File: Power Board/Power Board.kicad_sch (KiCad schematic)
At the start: 149 parts, among them IC1 LTC4151IMS#PBF, J1 Conn_01x02, J10 Conn_01x02, J11 Conn_01x02, J12 Conn_01x02, J13 Conn_01x02, J14 Conn_01x02, J15 Conn_01x02, J16 Conn_01x02, J17 Conn_01x02, J19 Conn_01x04, J2 Conn_01x02, J20 Conn_01x04, J3 Conn_01x02, J4 Conn_01x02, J5 Conn_01x02, J6 Conn_01x02, J7 Conn_01x02, J8 Conn_01x02, Q1 Q_PMOS_GDS, Q10 Q_NMOS_GDS, Q11 Q_NMOS_GDS, Q12 Q_NMOS_GDS, Q13 Q_NMOS_GDS, Q14 Q_NMOS_GDS, Q15 Q_NMOS_GDS, Q16 Q_NMOS_GDS, Q17 Q_NMOS_GDS, Q18 Q_NMOS_GDS, Q19 Q_NMOS_GDS, Q2 Q_PMOS_GDS, Q20 Q_NMOS_GDS, Q21 Q_NMOS_GDS, Q22 Q_NMOS_GDS, Q3 Q_PMOS_GDS, Q4 Q_PMOS_GDS, Q5 Q_PMOS_GDS, Q6 Q_PMOS_GDS, Q7 Q_PMOS_GDS, Q8 Q_PMOS_GDS, Q9 Q_NMOS_GDS, SW1 SW_Push_DPDT, U1 TLV70033_SOT23-5, U11 ACS770xCB-200U-PFF, U12 ADC128S052CIMT, U2 LTC4372CDD-PBF, U3 LTC4372CDD-PBF, U4 LTC4372CDD-PBF, U5 LTC4372CDD-PBF, U6 LTC4372CDD-PBF, U7 LTC4372CDD-PBF, U8 ADC128S052CIMT, U9 LTC4372CDD-PBF

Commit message: separated current sensors and updated ADCs, component numbering
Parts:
- removed C10: 10 uF, Capacitor_SMD:C_0201_0603Metric_Pad0.64x0.40mm_HandSolder, symbol Device:C
- removed J_Motor1, J_Motor2: Conn_01x02, Connector_AMASS:AMASS_XT60PW-F_1x02_P7.20mm_Horizontal, symbol Connector_Generic:Conn_01x02
- removed U11: ACS770xCB-200U-PFF, Sensor_Current:Allegro_CB_PFF, symbol Sensor_Current:ACS770xCB-200U-PFF
- added C30, C32, C34, C36, C38, C40: 0.1 uF, Capacitor_SMD:C_0201_0603Metric_Pad0.64x0.40mm_HandSolder, symbol Device:C
- added C31, C33, C35, C37, C39, C41: 1 uF, Capacitor_SMD:C_0201_0603Metric_Pad0.64x0.40mm_HandSolder, symbol Device:C
- added C42, C43, C44, C45, C46, C47, C48, C49, C50, C51, C52, C56: 22 nF, Capacitor_SMD:C_0201_0603Metric_Pad0.64x0.40mm_HandSolder, symbol Device:C
- added J_24_MONITOR1: Conn_01x02, symbol Connector_Generic:Conn_01x02
- added R43, R44, R45, R46, R47, R48, R49, R50, R51, R52: 100, Resistor_SMD:R_0805_2012Metric_Pad1.20x1.40mm_HandSolder, symbol Device:R
- added U10, U11, U12, U13, U14, U8, U9: ACS770xCB-050U-PFF, Sensor_Current:Allegro_CB_PFF, symbol Sensor_Current:ACS770xCB-050U-PFF
- R34: value 20k -> 100
- R35: value 10k -> 100
- renumbered J_PDB1 to J_BUS1, Q17 to Q10, Q13 to Q11, Q14 to Q12, Q9 to Q13, Q10 to Q14, Q11 to Q15, Q12 to Q16, Q21 to Q17, Q22 to Q18, Q15 to Q19, Q16 to Q20, Q19 to Q21, Q20 to Q22, Q18 to Q9, U9 to U1, U8 to U15, U12 to U16, U1 to U17, U4 to U2, U2 to U3, U3 to U4, U7 to U5, U5 to U6, U6 to U7
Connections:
- net +5V is gone; now on net 5V_REGULATED: C22.1, C23.1
- net 24V_MONITOR_SCL: now also J_24_MONITOR1.1 (Pin_1)
- net 24V_MONITOR_SDA: now also J_24_MONITOR1.2 (Pin_2)
- net 5V_REGULATED: now also C30.1, C31.1, C32.1, C33.1, C34.1, C35.1, C36.1, C37.1, C38.1, C39.1, C40.1, C41.1, U10.1 (VCC), U11.1 (VCC), U12.1 (VCC), U13.1 (VCC), U14.1 (VCC), U8.1 (VCC), U9.1 (VCC)
- net GND: now also C30.2, C31.2, C32.2, C33.2, C34.2, C35.2, C36.2, C37.2, C38.2, C39.2, C40.2, C41.2, C42.2, C43.2, C44.2, C45.2, C46.2, C47.2, C48.2, C49.2, C50.2, C51.2, C52.2, C56.2, U10.2 (GND), U11.2 (GND), U12.2 (GND), U13.2 (GND), U14.2 (GND), U8.2 (GND), U9.2 (GND); no longer R35.2
- net THERM_1: now also R49.1; no longer U16.4 (IN0)
- net THERM_2: now also R46.1; no longer U16.5 (IN1)
- net THERM_3: now also R47.1; no longer U16.6 (IN2)
- net THERM_4: now also R48.1; no longer U16.7 (IN3)
- net THERM_5: now also R50.1; no longer U16.8 (IN4)
- net THERM_6: now also R51.1; no longer U16.9 (IN5)
- net THERM_7: now also R52.1; no longer U16.10 (IN6)
- net THERM_8: no longer U16.11 (IN7)
- net at U15.10 (IN6): now also C46.1, R45.2
- net at U15.6 (IN2): now also R34.2, C42.1
- net at U15.7 (IN3): now also R35.2, C43.1
- net at U15.8 (IN4): now also C44.1, R43.2
- net at U15.9 (IN5): now also C45.1, R44.2
- net 12V_AMP_SENSE renamed BATT_1_SENSE
- net BATT_1_SENSE: now also U8.3 (VIOUT)
- removed net 12V_PRESENSE: Q11.2 (D), Q13.2 (D), Q15.2 (D), Q17.2 (D), Q19.2 (D), Q21.2 (D), Q9.2 (D), R34.1, U1.1 (OUT), U2.1 (OUT), U3.1 (OUT), U4.1 (OUT), U5.1 (OUT), U7.1 (OUT)
- net 12V_UNREGULATED: no longer names the net of J_BUS1.2 (Pin_2)
- new net: C47.1, R46.2, U16.5 (IN1)
- new net: C52.1, R51.2, U16.9 (IN5)
- new net: C51.1, R50.2, U16.8 (IN4)
- new net: C56.1, R52.2, U16.10 (IN6)
- new net: C50.1, R49.2, U16.4 (IN0)
- new net: C48.1, R47.2, U16.6 (IN2)
- new net: C49.1, R48.2, U16.7 (IN3)
- new net BATT_1: U8.5 (IP-)
- new net BATT_1_PRESENSE: Q9.2 (D), U1.1 (OUT), U8.4 (IP+)
- new net BATT_2: U9.5 (IP-)
- new net BATT_2_PRESENSE: Q11.2 (D), U2.1 (OUT), U9.4 (IP+)
- new net BATT_2_SENSE: R2.1, U9.3 (VIOUT)
- new net BATT_3: U10.5 (IP-)
- new net BATT_3_PRESENSE: Q13.2 (D), U10.4 (IP+), U3.1 (OUT)
- new net BATT_3_SENSE: R34.1, U10.3 (VIOUT)
- new net BATT_4: U11.5 (IP-)
- new net BATT_4_PRESENSE: Q15.2 (D), U11.4 (IP+), U4.1 (OUT)
- new net BATT_4_SENSE: R35.1, U11.3 (VIOUT)
- new net BATT_5: U12.5 (IP-)
- new net BATT_5_PRESENSE: Q17.2 (D), U12.4 (IP+), U5.1 (OUT)
- new net BATT_5_SENSE: R43.1, U12.3 (VIOUT)
- new net BATT_6: U13.5 (IP-)
- new net BATT_6_PRESENSE: Q19.2 (D), U13.4 (IP+)
- new net BATT_6_SENSE: R44.1, U13.3 (VIOUT)
- new net BATT_7: U14.5 (IP-)
- new net BATT_7_PRESENSE: Q21.2 (D), U14.4 (IP+), U7.1 (OUT)
- new net BATT_7_SENSE: R45.1, U14.3 (VIOUT)
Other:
- note added: "Current Monitors"
- moved on the sheet: C2, C21, C22, C23, C26, C27, IC1, J10, J11, J12, J13, J14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

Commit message: updated schematic numbering, made rough PCB design for battery 1
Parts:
- renumbered C11 to C1, C17 to C10, C8 to C11, C14 to C12, C9 to C13, C15 to C14, C2 to C15, C1 to C16, C42 to C17, C43 to C18, C44 to C19, C12 to C2, C45 to C20, C46 to C21, C20 to C22, C18 to C23, C19 to C24, C50 to C25, C47 to C26, C48 to C27, C49 to C28, C51 to C29, C7 to C3, C52 to C30, C56 to C31, C21 to C32, C26 to C33, C27 to C34, C22 to C35, C23 to C36, C30 to C37, C31 to C38, C40 to C39, C13 to C4, C41 to C40, C32 to C41, C33 to C42, C34 to C43, C35 to C44, C36 to C45, C37 to C46, C38 to C47, C39 to C48, C28 to C49, C3 to C5, C29 to C50, C25 to C51, C24 to C52, C4 to C6, C5 to C7, C6 to C8, C16 to C9, R5 to R1, R21 to R10, R22 to R11, R19 to R12, R25 to R13, R28 to R14, R13 to R15, R14 to R16, R15 to R17, R16 to R18, R17 to R19, R6 to R2, R18 to R20, R31 to R21, R32 to R22, R33 to R23, R23 to R24, R26 to R25, R29 to R26, R24 to R27, R27 to R28, R30 to R29, R7 to R3, R8 to R4, R9 to R5, R10 to R6, R11 to R7, R12 to R8, R20 to R9, R3 to RA1, R47 to RA10, R48 to RA11, R50 to RA12, R51 to RA13, R52 to RA14, R2 to RA2, R34 to RA3, R35 to RA4, R43 to RA5, R44 to RA6, R45 to RA7, R49 to RA8, R46 to RA9, R1 to RI1, R4 to RT1, R36 to RT2, R37 to RT3, R38 to RT4, R39 to RT5, R40 to RT6, R41 to RT7, R42 to RT8

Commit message: adc design on power board
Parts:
- removed C51, C52: UVZ2A331MHD1TO, UVZ2A331MHD:CAP_UEP_12P5X25_NCH, symbol 2025-11-07_01-42-20:UVZ2A331MHD1TO
- added C51, C52: EEV-TG2A331M, EEV_TG2A331M:CAP_SMD_19X19_PAN, symbol EEV_TG2A331M:EEV-TG2A331M
- added NT1: NetTie_2, symbol Device:NetTie_2
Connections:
- net 24V_PRESENSE is gone; now on net 24V_PSO: IC1.1 (SENSE+), IC1.2 (VIN), IC1.3 (ADR1), RI1.1
- net 24_REGULATED is gone; now on net 24V_REGULATED: PS1.4 (+VOUT)
- net 24V_UNREGULATED: now also C51.2, C52.1
- net GND: now also C23.2, C24.2, C33.2, C34.2, C51.1, C52.2, NT1.1
- net GNDD: now also NT1.2

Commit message: laid out most components, reworked battery 1 pours, made connections for ADCs; buck converter layout and routing in progress
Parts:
- removed Q1, Q2, Q3, Q4, Q5, Q6, Q7, Q8: Q_PMOS_GDS, Package_SO:PowerPAK_SO-8_Single, symbol Device:Q_PMOS_GDS
- added Q1, Q2, Q3, Q4, Q5, Q6, Q7, Q8: Q_PMOS_GDS, Package_SO:PowerPAK_SO-8_Single, symbol Transistor_FET:Q_PMOS_GDS
- Q10, Q11, Q12, Q13, Q14, Q15, Q16, Q17, Q18, Q19, Q20, Q21, Q22, Q9: footprint Package_TO_SOT_SMD:TDSON-8-1 -> Package_SO:PowerPAK_SO-8_Single
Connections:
- net 24V_PSO: now also Q8.3 (S)
- net ADC_1_DIN: now also J20.4 (Pin_4); no longer J20.3 (Pin_3)
- net ADC_1_DOUT: now also J20.2 (Pin_2); no longer J20.4 (Pin_4)
- net ADC_1_SCLK: now also J20.3 (Pin_3); no longer J20.2 (Pin_2)
- net ADC_2_DIN: now also J19.4 (Pin_4); no longer J19.3 (Pin_3)
- net ADC_2_DOUT: now also J19.2 (Pin_2); no longer J19.4 (Pin_4)
- net ADC_2_SCLK: now also J19.3 (Pin_3); no longer J19.2 (Pin_2)
- net BATT_IN_12_1: now also Q1.3 (S)
- net BATT_IN_12_2: now also Q2.3 (S)
- net BATT_IN_12_3: now also Q3.3 (S)
- net BATT_IN_12_4: now also Q4.3 (S)
- net BATT_IN_12_5: now also Q5.3 (S)
- net BATT_IN_12_6: now also Q6.3 (S)
- net BATT_IN_12_7: now also Q7.3 (S)
- net GND: now also U1.9 (GND), U2.9 (GND), U3.9 (GND), U4.9 (GND), U5.9 (GND), U6.9 (GND), U7.9 (GND); no longer C22.2, C32.2
- net GNDD: now also C22.2, C32.2
- net at D5.2 (A), R5.1: now also Q5.1 (G)
- net at F5.2: now also Q5.2 (D)
- net at D4.2 (A), R4.1: now also Q4.1 (G)
- net at F8.2: now also Q8.2 (D)
- net at F7.2: now also Q7.2 (D)
- net at D7.2 (A), R7.1: now also Q7.1 (G)
- net at D3.2 (A), R3.1: now also Q3.1 (G)
- net at D6.2 (A), R6.1: now also Q6.1 (G)
- net at D8.2 (A), R8.1: now also Q8.1 (G)
- net at D1.2 (A), R1.1: now also Q1.1 (G)
- net at F1.2: now also Q1.2 (D)
- net at F4.2: now also Q4.2 (D)
- net at D2.2 (A), R2.1: now also Q2.1 (G)
- net at F2.2: now also Q2.2 (D)
- net at F3.2: now also Q3.2 (D)
- net at F6.2: now also Q6.2 (D)
- no-connect marks 0 -> 9
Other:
- moved on the sheet: C49, C50, U17

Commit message: changed ADC connectors, added series resistors
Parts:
- removed J19, J20: Conn_01x04, Connector_Molex:Molex_Micro-Fit_3.0_43045-0400_2x02_P3.00mm_Horizontal, symbol Connector_Generic:Conn_01x04
- added J18: Conn_02x03_Top_Bottom, Connector_Molex:Molex_Nano-Fit_105310-xx06_2x03_P2.50mm_Vertical, symbol Connector_Generic:Conn_02x03_Top_Bottom
- added J20, J9: Conn_02x03_Top_Bottom, Connector_Molex:Molex_Nano-Fit_105314-xx06_2x03_P2.50mm_Horizontal, symbol Connector_Generic:Conn_02x03_Top_Bottom
- added R30, R31, R32, R33, R34, R35, R36, R37: 33, Resistor_SMD:R_0805_2012Metric_Pad1.20x1.40mm_HandSolder, symbol Device:R
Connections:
- net 24V_PSO: now also C52.1, D9.1 (K), PS2.1 (+VIN), J18.1 (Pin_1)
- net 24V_UNREGULATED: now also J18.2 (Pin_2); no longer C52.1, D9.1 (K), PS2.1 (+VIN)
- net 5V_REG_SD: now also J18.6 (Pin_6)
- net ADC_1_CS: now also R30.2
- net ADC_1_DIN: now also R32.2
- net ADC_1_DOUT: now also R31.2
- net ADC_1_SCLK: now also R33.1
- net ADC_2_CS: now also R37.2
- net ADC_2_DIN: now also R35.2
- net ADC_2_DOUT: now also R36.2
- net ADC_2_SCLK: now also R34.1
- net GND: now also J18.4 (Pin_4)
- net GNDD: now also J20.2 (Pin_2), J20.5 (Pin_5), J9.2 (Pin_2), J9.5 (Pin_5)
- net SHDN: now also J18.5 (Pin_5)
- new net: J9.4 (Pin_4), R30.1
- new net: J9.1 (Pin_1), R33.2
- new net: J9.3 (Pin_3), R32.1
- new net: J20.3 (Pin_3), R35.1
- new net: J9.6 (Pin_6), R31.1
- new net: J20.1 (Pin_1), R34.2
- new net: J20.4 (Pin_4), R37.1
- new net: J20.6 (Pin_6), R36.1
- no-connect marks 9 -> 10
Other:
- moved on the sheet: SW1

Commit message: updated LTC4372s, switch connector, ADC; added some power planes for other batteries
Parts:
- removed SW1: SW_Push_DPDT, symbol Switch:SW_Push_DPDT
- added C53: 22 nF, Capacitor_SMD:C_0201_0603Metric_Pad0.64x0.40mm_HandSolder, symbol Device:C
- added RA15: 100, Resistor_SMD:R_0805_2012Metric_Pad1.20x1.40mm_HandSolder, symbol Device:R
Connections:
- net 24V_PSO: no longer C52.1, D9.1 (K), PS2.1 (+VIN)
- net 24V_UNREGULATED: now also C52.1, D9.1 (K), PS2.1 (+VIN)
- net BATT_IN_12_2: now also Q12.2 (D), U2.4 (IN); no longer Q14.2 (D), U3.4 (IN)
- net BATT_IN_12_3: now also Q14.2 (D), U3.4 (IN); no longer Q16.2 (D), U4.4 (IN)
- net BATT_IN_12_4: now also Q16.2 (D), U4.4 (IN); no longer Q12.2 (D), U2.4 (IN)
- net BATT_IN_12_5: now also Q18.2 (D), U5.4 (IN); no longer Q20.2 (D), U6.4 (IN)
- net BATT_IN_12_6: now also Q20.2 (D), U6.4 (IN); no longer Q22.2 (D), U7.4 (IN)
- net BATT_IN_12_7: now also Q22.2 (D), U7.4 (IN); no longer Q18.2 (D), U5.4 (IN)
- net GND: now also C53.2
- net SHDN: now also U1.7 (2UPU), U2.7 (2UPU), U3.7 (2UPU), U4.7 (2UPU), U5.7 (2UPU), U6.7 (2UPU), U7.7 (2UPU)
- net THERM_8: now also RA15.1
- net at U16.11 (IN7): now also C53.1, RA15.2
- net 5V_REG_SD: no longer names the net of J18.6 (Pin_6)
- no-connect marks 10 -> 9

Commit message: more layout, power planes for 24V and 5V rails, current sensing and switch connections; might move digital section with ADCs and LTC4151s to bottom left
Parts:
- removed J_24_MONITOR1: Conn_01x02, symbol Connector_Generic:Conn_01x02
- added IC2: LTC4151IMS#PBF, Package_SO:MSOP-10_3x3mm_P0.5mm, symbol LTC4151IMS#PBF:LTC4151IMS#PBF
- added J_BMS1: Conn_01x04, symbol Connector_Generic:Conn_01x04
- added J_I2C_Jetson1: Conn_02x02_Counter_Clockwise, symbol Connector_Generic:Conn_02x02_Counter_Clockwise
- added RI2: 0.04, Resistor_SMD:R_0805_2012Metric_Pad1.20x1.40mm_HandSolder, symbol Device:R
- IC1: footprint LTC4151:MSOP-10_MS_LIT -> Package_SO:MSOP-10_3x3mm_P0.5mm
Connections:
- net 24V_PSO: no longer IC1.1 (SENSE+), IC1.2 (VIN), IC1.3 (ADR1), RI1.1
- net 24V_REGULATED: now also IC1.10 (SENSE-), RI1.2; no longer PS1.4 (+VOUT)
- net 24V_UNREGULATED: no longer IC1.10 (SENSE-), RI1.2
- net 5V_REGULATED: now also IC2.10 (SENSE-), RI2.2; no longer PS2.6 (-VOUT)
- net GND: now also IC2.3 (ADR1), IC2.4 (ADR0), IC2.5 (ADIN), IC2.9 (GND)
- net GNDD: now also J_BMS1.1 (Pin_1), J_BMS1.3 (Pin_3), J_I2C_Jetson1.2 (Pin_2), J_I2C_Jetson1.3 (Pin_3)
- net 24V_MONITOR_SCL renamed SCL
- net SCL: now also IC2.6 (SCL), J_BMS1.4 (Pin_4), J_I2C_Jetson1.1 (Pin_1)
- net 24V_MONITOR_SDA renamed SDA
- net SDA: now also IC2.7 (SDA), J_BMS1.2 (Pin_2), J_I2C_Jetson1.4 (Pin_4)
- new net 24V_PRESENSE: IC1.1 (SENSE+), IC1.2 (VIN), PS1.4 (+VOUT), RI1.1
- new net 5V_PSO: IC2.1 (SENSE+), IC2.2 (VIN), PS2.6 (-VOUT), RI2.1
- no-connect marks 9 -> 10
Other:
- note added: "Battery Monitors (5V and 24V)"
- note added: "Hex Address: D6"
- note added: "Hex Address: DE"
- note removed: "Battery Monitor"
- moved on the sheet: IC1, J10, J11, J12, J13, J14, J15, J16, J17, NT1, RI1, RT1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

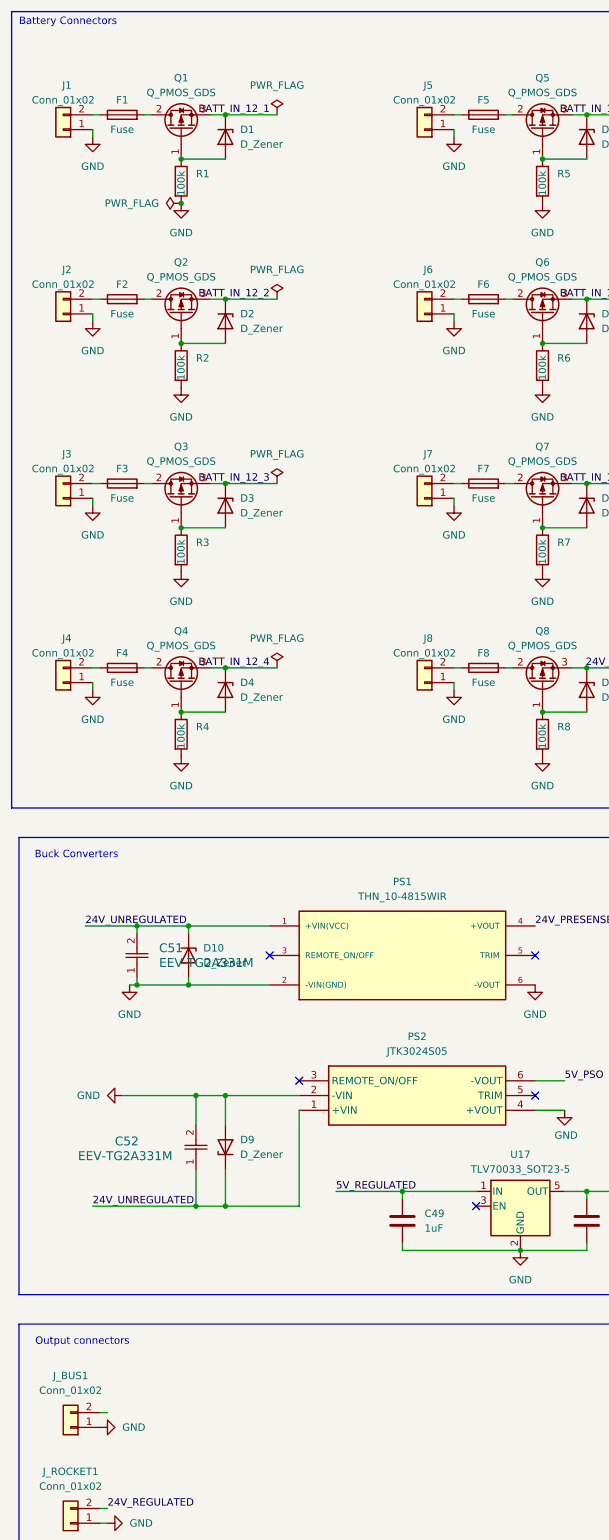
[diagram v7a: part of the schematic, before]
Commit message: updated xt60 connectors, routed ADC lines
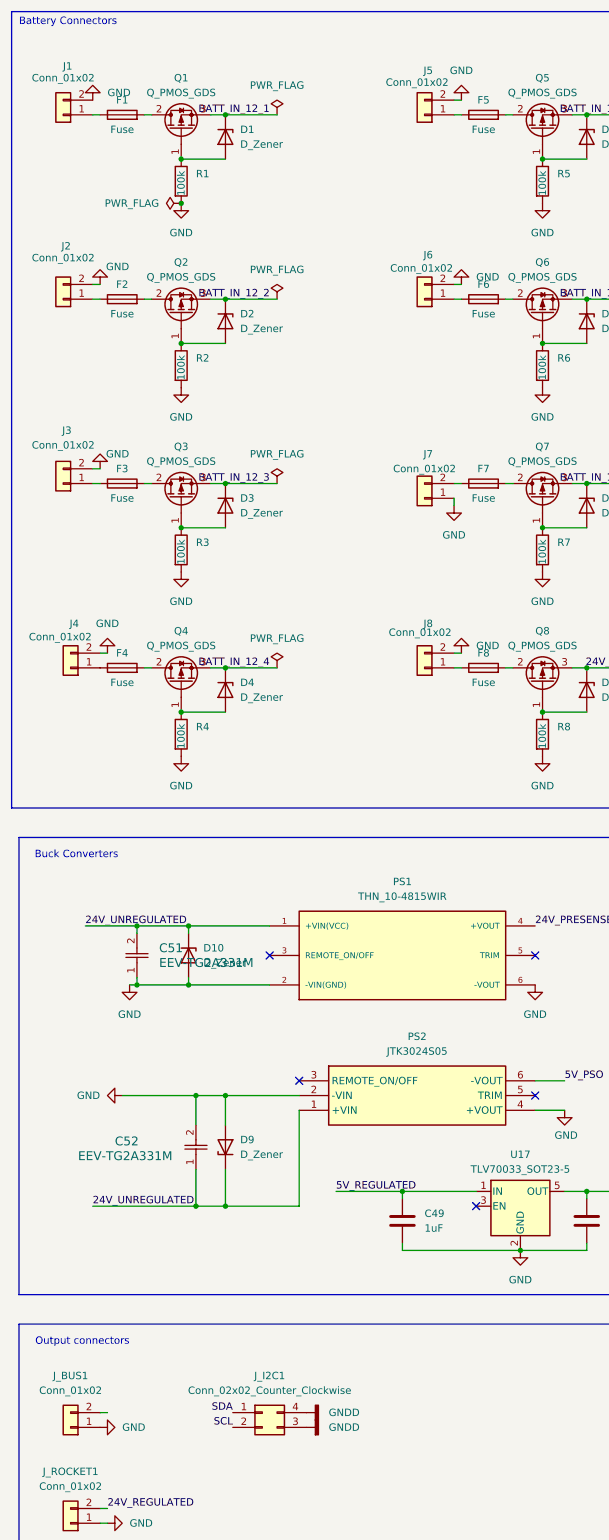
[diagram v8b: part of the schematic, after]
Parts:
- added J_I2C1: Conn_02x02_Counter_Clockwise, Connector_Molex:Molex_Nano-Fit_105309-xx04_1x04_P2.50mm_Vertical, symbol Connector_Generic:Conn_02x02_Counter_Clockwise
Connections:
- net GND: now also J1.2 (Pin_2), J2.2 (Pin_2), J3.2 (Pin_2), J4.2 (Pin_2), J5.2 (Pin_2), J6.2 (Pin_2), J8.2 (Pin_2); no longer J1.1 (Pin_1), J2.1 (Pin_1), J3.1 (Pin_1), J4.1 (Pin_1), J5.1 (Pin_1), J6.1 (Pin_1), J8.1 (Pin_1)
- net GNDD: now also J_I2C1.3 (Pin_3), J_I2C1.4 (Pin_4)
- net SCL: now also J_I2C1.2 (Pin_2)
- net SDA: now also J_I2C1.1 (Pin_1)
- net at F8.1: now also J8.1 (Pin_1); no longer J8.2 (Pin_2)
- net at F2.1: now also J2.1 (Pin_1); no longer J2.2 (Pin_2)
- net at F4.1: now also J4.1 (Pin_1); no longer J4.2 (Pin_2)
- net at F3.1: now also J3.1 (Pin_1); no longer J3.2 (Pin_2)
- net at F1.1: now also J1.1 (Pin_1); no longer J1.2 (Pin_2)
- net at F5.1: now also J5.1 (Pin_1); no longer J5.2 (Pin_2)
- net at F6.1: now also J6.1 (Pin_1); no longer J6.2 (Pin_2)
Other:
- moved on the sheet: J1, J2, J3, J4, J5, J6, J8
